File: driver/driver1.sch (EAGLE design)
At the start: 85 parts, among them IC3 74HC14N, IC4 74HC08N, IC5 74HC74N

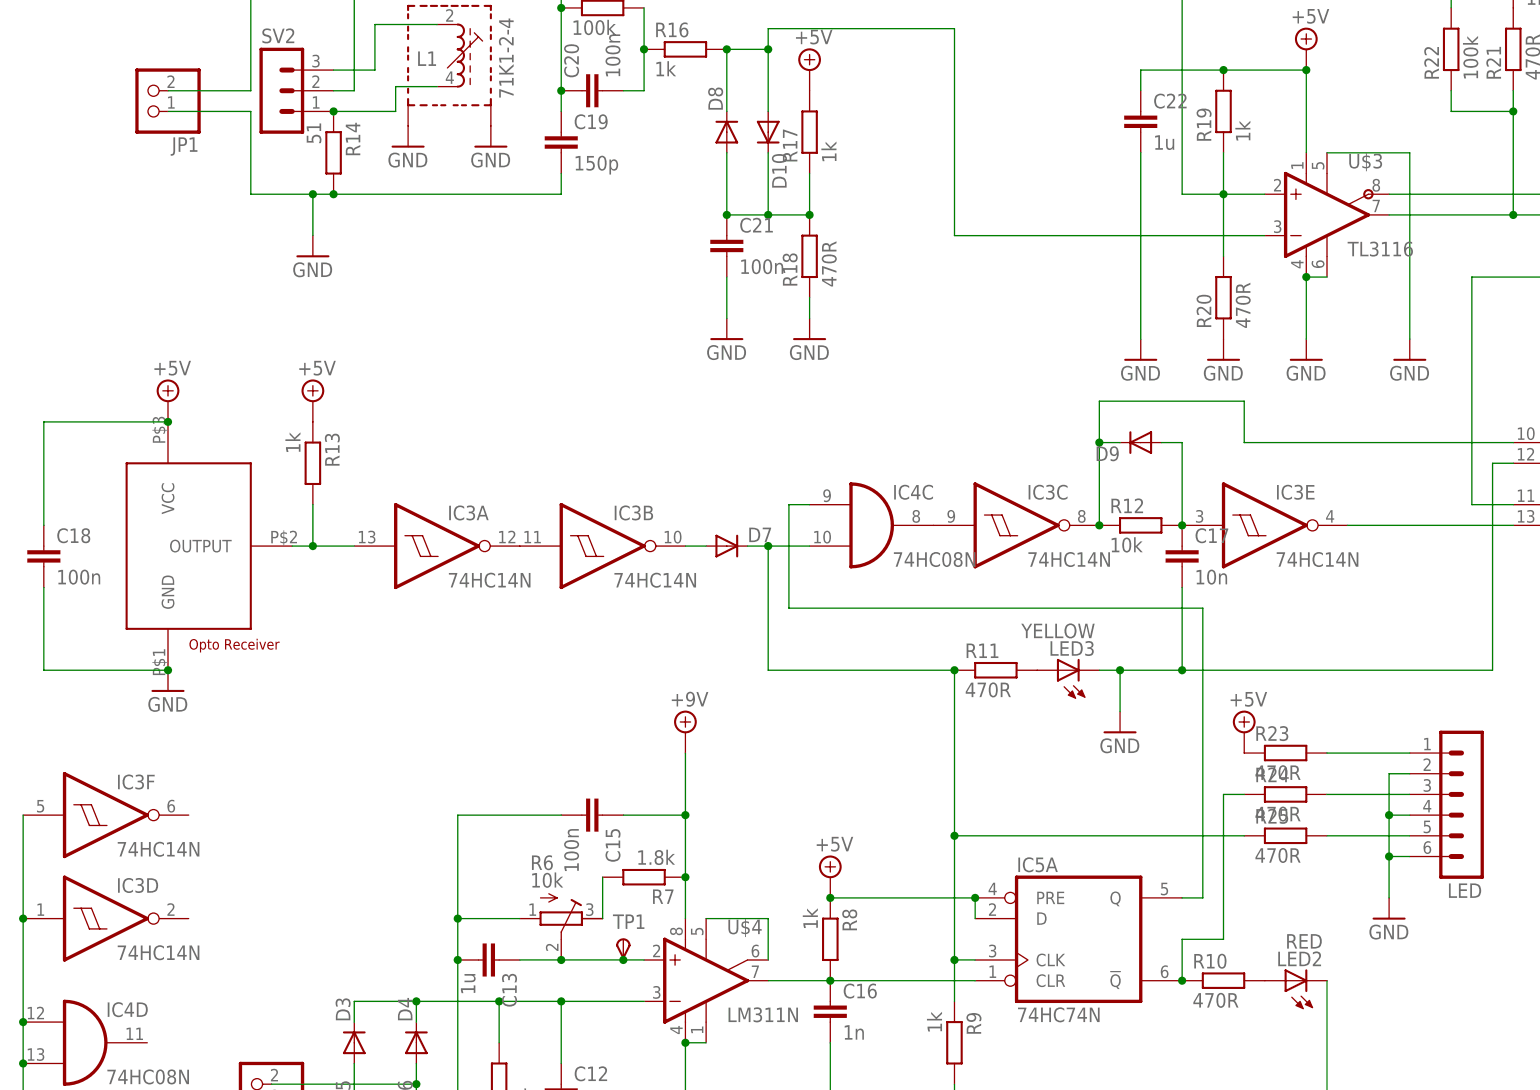
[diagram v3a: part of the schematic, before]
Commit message: added missing prefix to libraries
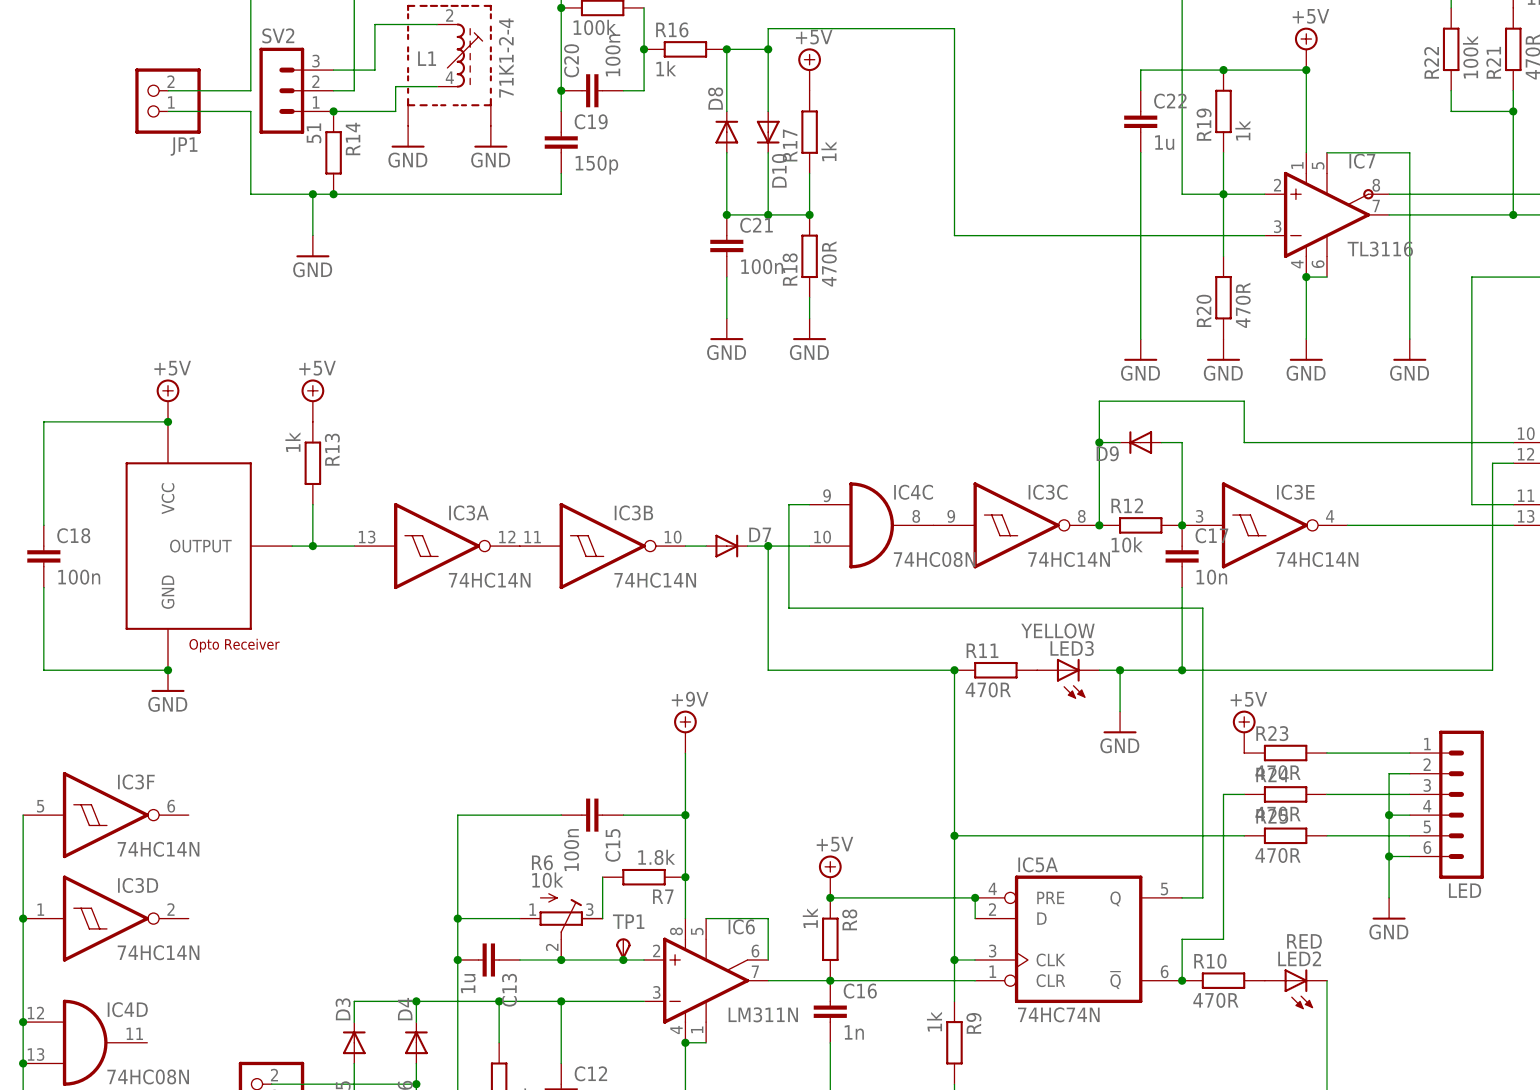
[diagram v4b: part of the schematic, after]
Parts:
- renumbered U$1 to IC8, U$2 to OP1, U$3 to IC7, U$4 to IC6
